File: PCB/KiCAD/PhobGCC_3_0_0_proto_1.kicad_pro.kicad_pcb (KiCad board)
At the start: 2 copper layers, 125.5 x 90.3 mm, 113 parts, among them J1 Conn_01x06_Female, J11 Conn_01x02, J14 Conn_01x06, J15 Conn_01x06, J2 Conn_01x02, J3 Conn_01x02, J4 Conn_01x01, J5 Rumble, J6 Conn_01x06, J8 USB_B_Micro, Q1 Q_NMOS_GSD, Q2 Q_PMOS_GDS, Q3 Q_NMOS_GSD, SW1 A, SW10 Dup, SW11 Dright, SW12 Ddown, SW2 B, SW3 X, SW4 Y, SW5 Start, SW6 L, SW7 R, SW8 Z, SW9 Dleft, U1 MCP3202, U10 DRV5055A3xDBZxQ1, U11 DRV5055A3xDBZxQ1, U12 USBLC6-2P6, U13 USBLC6-2P6, U2 Stickbox_Assembly_Main, U3 MCP3202, U4 DRV5055A3xDBZxQ1, U5 Stickbox_Assembly_CStick, U6 AMS1117-3.3, U7 W25Q128JVS, U8 RP2040, U9 DRV5055A3xDBZxQ1, Y1 Crystal_GND24

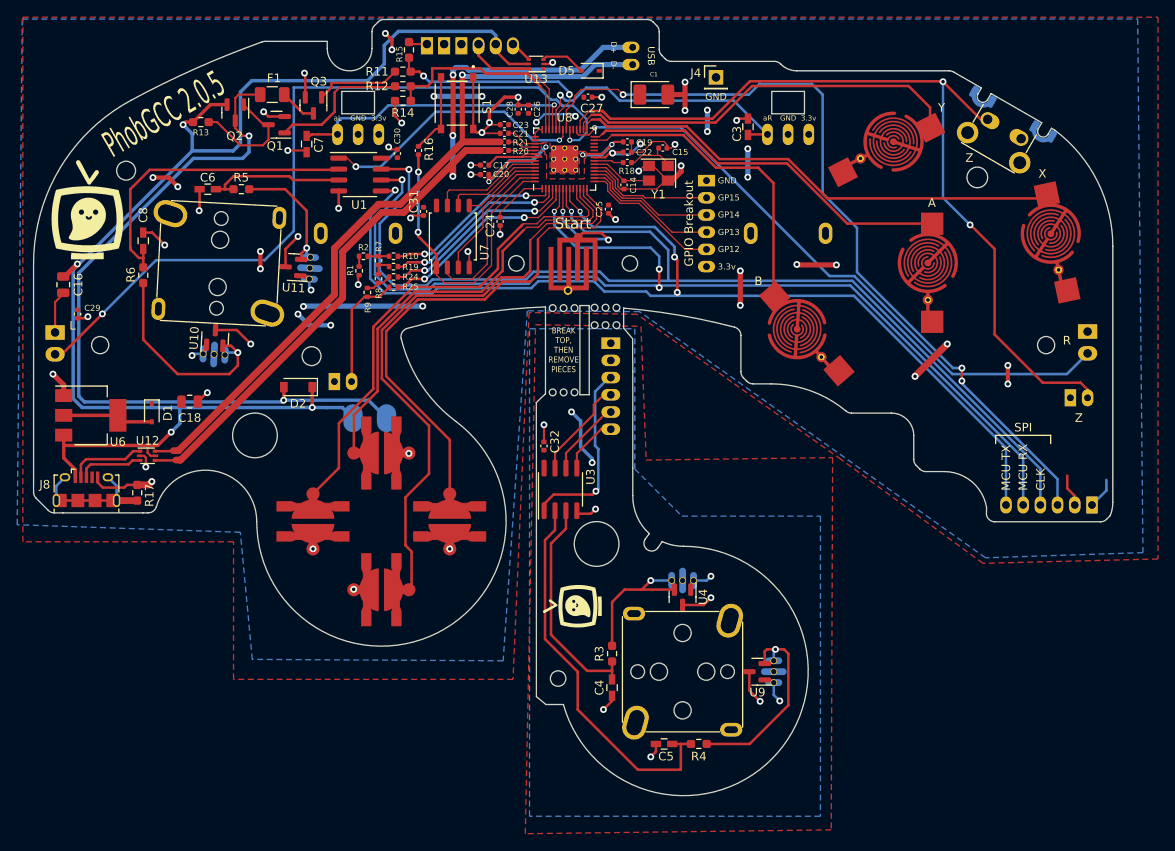
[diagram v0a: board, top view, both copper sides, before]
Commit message: RP2040 to RP2350 Conversion
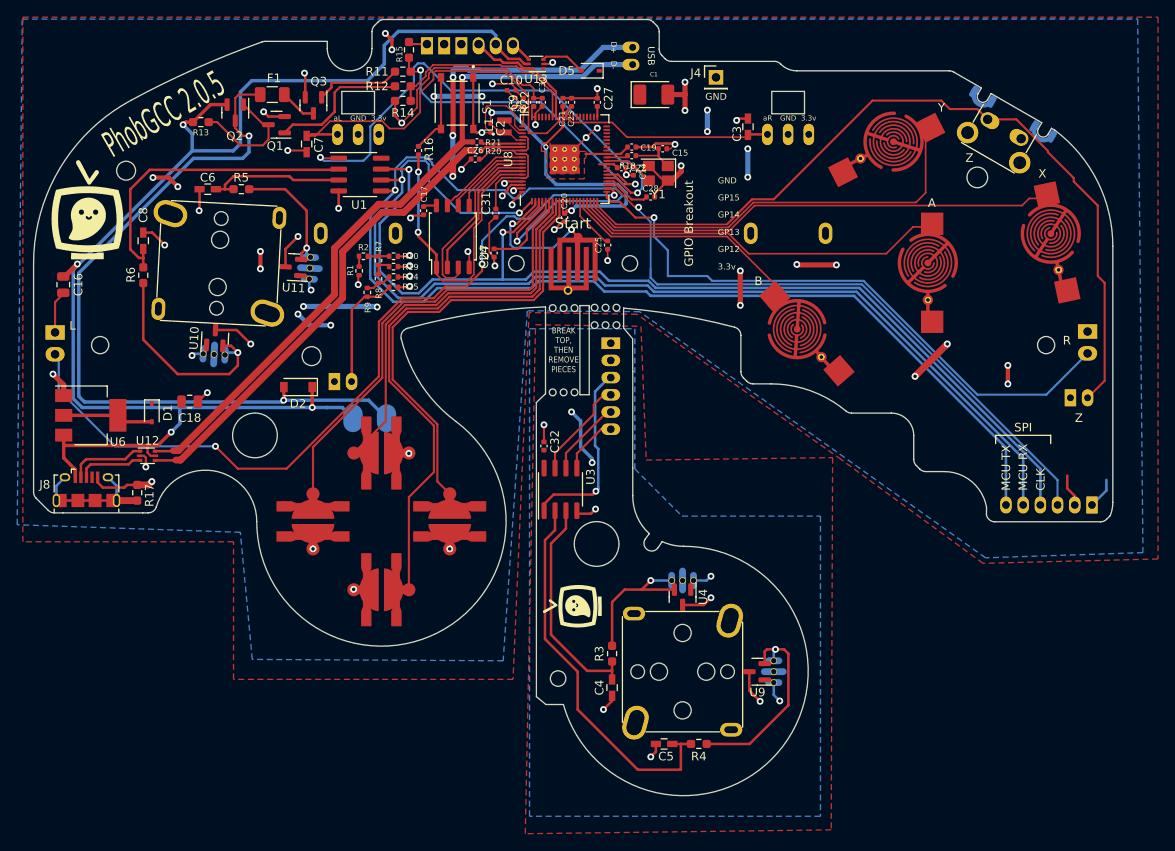
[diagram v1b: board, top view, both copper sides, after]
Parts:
- removed J6: Conn_01x06, Connector_PinSocket_2.00mm:PinSocket_1x06_P2.00mm_Vertical
- added C10: 4.7u, RP2350_80QFN_minimal:C_0402_1005Metric_small_pads, F.Cu at (103.8, 31.0)
- added C2: 4.7u, RP2350_80QFN_minimal:C_0402_1005Metric_small_pads, F.Cu at (101.4, 35.4)
- added C9: 4.7u, Capacitor_SMD:C_0402_1005Metric, F.Cu at (105.2, 32.4)
- added L1: 3.3u, RP2350_80QFN_minimal:L_pol_2016, F.Cu at (103.0, 35.2)
- added R22: 33, Resistor_SMD:R_0402_1005Metric, F.Cu at (104.2, 32.4)
- C21: value 1u -> 4.7u
- U8: value RP2040 -> RP2350; footprint PhobGCC_2_0_0_footprints:RP2040-QFN-56 -> RP2350_80QFN_minimal:RP2350-QFN-80-1EP_10x10_P0.4mm_EP3.4x3.4mm_ThermalVias
- moved C29 58.5 mm to (106.4, 32.4), turned to 90 degrees
- moved C28 18.5 mm to (120.0, 43.4), turned to 0 degrees
- moved C30 17.9 mm to (107.4, 32.4)
- moved C20 10.6 mm to (110.0, 45.8), turned to -90 degrees
- moved C17 8.86 mm to (93.6, 45.0), turned to -90 degrees
- moved C26 8.49 mm to (99.6, 39.0), turned to 180 degrees
- moved C31 8.40 mm to (102.0, 45.3)
- moved C23 8.22 mm to (110.8, 32.4), turned to 90 degrees
- moved C21 7.69 mm to (109.8, 32.4), turned to 90 degrees
- moved C25 4.18 mm to (115.0, 49.0)
- moved C24 3.74 mm to (101.8, 49.9)
- moved R20 3.20 mm to (99.8, 38.0)
- moved R21 3.20 mm to (99.8, 37.0)
- moved C14 1.94 mm to (118.0, 40.4)
- moved C22 1.93 mm to (116.6, 40.0)
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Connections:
- R20 pad 2: Net-(R20-Pad2) -> Net-(U8-USB_DP)
- R21 pad 2: Net-(R21-Pad2) -> Net-(U8-USB_DM)
- U8 pad 1: +3V3 -> /Dout
- U8 pad 10: +3V3 -> +1V1
- U8 pad 11: /Dleft -> /GPIO12
- U8 pad 12: /Dup -> /GPIO13
- U8 pad 13: /Ddown -> /GPIO14
- U8 pad 14: /Dright -> /GPIO15
- U8 pad 15: /GPIO12 -> +3V3
- U8 pad 16: /GPIO13 -> /B
- U8 pad 17: /GPIO14 -> /A
- U8 pad 18: /GPIO15 -> /X
- U8 pad 19: GND -> /Y
- U8 pad 2: /Ladder1 -> /Start
- U8 pad 20: /XIN -> /Z
- U8 pad 21: /XOUT -> /R
- U8 pad 22: +3V3 -> /L
- U8 pad 23: +1V1 -> /CS2
- U8 pad 24: /SWCLK -> +3V3
- U8 pad 25: /SWD -> /CS1
- U8 pad 26: /RUN -> /Rumble
- U8 pad 27: /B -> unconnected-(U8-GPIO26-Pad27)
- U8 pad 28: /A -> unconnected-(U8-GPIO27-Pad28)
- U8 pad 29: /X -> +3V3
- U8 pad 3: /Ladder2 -> /CLK
- U8 pad 30: /Y -> /XIN
- U8 pad 31: /Z -> /XOUT
- U8 pad 32: /R -> +1V1
- U8 pad 33: +3V3 -> /SWCLK
- U8 pad 34: /L -> /SWD
- U8 pad 35: /CS2 -> /RUN
- U8 pad 36: /CS1 -> unconnected-(U8-GPIO28-Pad36)
- U8 pad 37: /Rumble -> unconnected-(U8-GPIO29-Pad37)
- U8 pad 38: /Ranalog -> unconnected-(U8-GPIO30-Pad38)
- U8 pad 39: /Lanalog -> unconnected-(U8-GPIO31-Pad39)
- U8 pad 4: /Ladder3 -> /Din
- U8 pad 40: /GCC_DATA -> unconnected-(U8-GPIO32-Pad40)
- U8 pad 41: /Brake -> +3V3
- U8 pad 42: +3V3 -> unconnected-(U8-GPIO33-Pad42)
- U8 pad 43: +3V3 -> unconnected-(U8-GPIO34-Pad43)
- U8 pad 44: +3V3 -> unconnected-(U8-GPIO35-Pad44)
- U8 pad 45: +1V1 -> unconnected-(U8-GPIO36-Pad45)
- U8 pad 46: Net-(R21-Pad2) -> unconnected-(U8-GPIO37-Pad46)
- U8 pad 47: Net-(R20-Pad2) -> unconnected-(U8-GPIO38-Pad47)
- U8 pad 48: +3V3 -> unconnected-(U8-GPIO39-Pad48)
- U8 pad 49: +3V3 -> /Ranalog
- U8 pad 5: /Ladder4 -> +3V3
- U8 pad 50: +1V1 -> +3V3
- U8 pad 51: /QSPI_SD3 -> +1V1
- U8 pad 52: /QSPI_SCLK -> /Lanalog
- U8 pad 53: /QSPI_SD0 -> /GCC_DATA
- U8 pad 54: /QSPI_SD2 -> /Brake
- U8 pad 55: /QSPI_SD1 -> unconnected-(U8-GPIO44_ADC4-Pad55)
- U8 pad 56: /QSPI_SS -> unconnected-(U8-GPIO45_ADC5-Pad56)
- U8 pad 57: GND -> unconnected-(U8-GPIO46_ADC6-Pad57)
- U8 pad 6: /Dout -> /Dleft
- U8 pad 7: /Start -> /Dup
- U8 pad 8: /CLK -> /Ddown
- U8 pad 9: /Din -> /Dright
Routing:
- net GND: track 140.9 -> 187.7 mm, vias 51 -> 50
- net /Din: track 125.5 -> 156.4 mm, vias 4 -> 2
- net /CS1: track 32.4 -> 59.3 mm
- net +3V3: track 66.6 -> 91.0 mm, vias 16 -> 13
- net /CS2: track 94.4 -> 73.5 mm, vias 3 -> 1
- net +1V1: track 29.3 -> 47.5 mm, vias 4 -> 3
- net /GPIO12: track 17.0 -> 0.00 mm
- net /GPIO13: track 16.3 -> 0.00 mm
- net /GPIO14: track 15.7 -> 0.00 mm
- net /GPIO15: track 15.0 -> 0.00 mm
- net /Rumble: track 26.0 -> 38.3 mm
- net /Lanalog: track 34.2 -> 45.4 mm, vias 1 -> 0
- net /Ranalog: track 33.7 -> 23.9 mm, vias 1 -> 0
- net /B: track 37.2 -> 28.8 mm
- net /CLK: track 128.3 -> 120.5 mm
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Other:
- copper layers 2 -> 4
